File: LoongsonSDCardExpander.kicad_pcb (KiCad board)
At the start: 2 copper layers, 42.1 x 32.7 mm, 30 parts, among them J1 USB_C_Receptacle_USB2.0, J2 Micro_SD_Card_Det, J3 Conn_02x10_Odd_Even, U1 CH340E

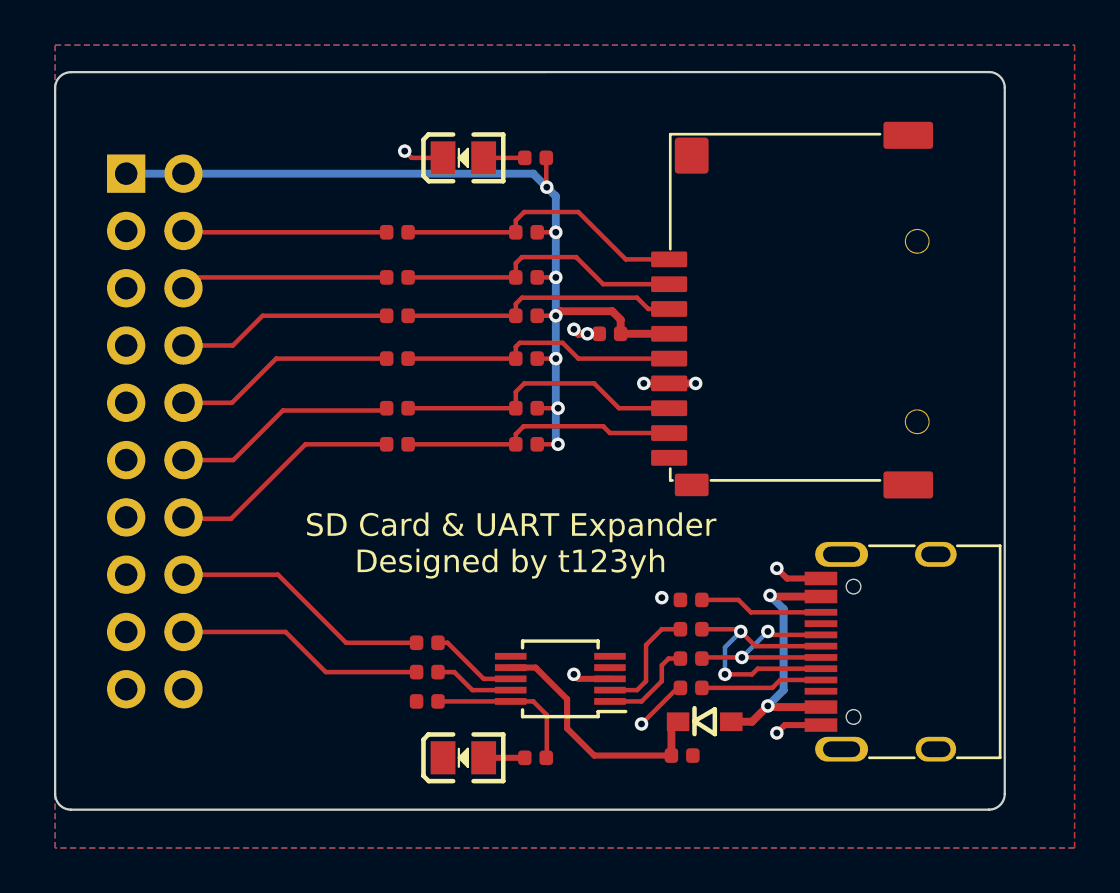
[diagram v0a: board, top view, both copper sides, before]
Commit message: 添加Conn_01x11_Socket
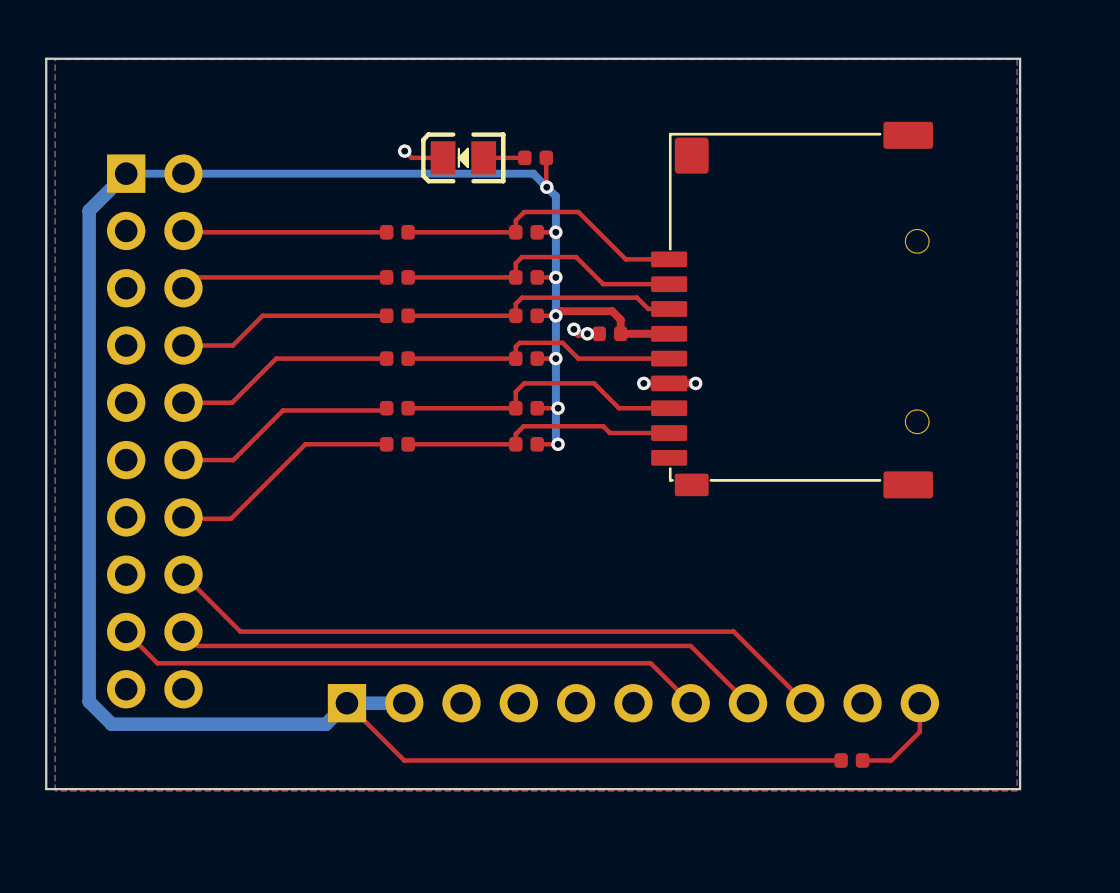
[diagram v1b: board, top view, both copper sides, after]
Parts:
- removed C1: 2.2uF, lc:0402_C
- removed C2: 100nF, lc:0402_C
- removed D1: 1N5819WS, lc:SOD-323
- removed D3: Green, lc:0805_LED_S1_NUM
- removed J1: USB_C_Receptacle_USB2.0, t123yh:USB_C_Receptacle_HRO_TYPE-C-31-M-12
- removed R1, R2: 5.1k, lc:0402_R
- removed R13, R14, R3, R4: 22, lc:0402_R
- removed R20: 22k, lc:0402_R
- removed U1: CH340E, Package_SO:MSOP-10_3x3mm_P0.5mm
- added J4: Conn_01x11_Socket, Connector_PinSocket_2.54mm:PinSocket_1x11_P2.54mm_Vertical, B.Cu at (66.0, 157.5)
- added R21: 47k, lc:0402_R, F.Cu at (88.4, 160.0)
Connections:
- J3 pad 16: /TX -> /I2S_LCK
- J3 pad 17: unconnected-(J3-Pad17) -> /I2S_BCK
- J3 pad 18: /RX -> /I2S_DIN
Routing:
- net +3.3V: track 42.8 -> 104.6 mm
- net /I2S_LCK: track 0.00 -> 29.9 mm
- net /I2S_BCK: track 0.00 -> 26.3 mm
- net /I2S_DIN: track 0.00 -> 26.3 mm
- net Net-(J1-PadA7): track 12.1 -> 0.00 mm, vias 2 -> 0
- net Net-(D1-Pad2): track 12.0 -> 0.00 mm, vias 2 -> 0
- net /TX: track 11.6 -> 0.00 mm
- net Net-(C1-Pad1): track 11.1 -> 0.00 mm
- net /RX: track 11.1 -> 0.00 mm
- net Net-(J1-PadA6): track 9.34 -> 0.00 mm, vias 2 -> 0
- net GND: track 13.6 -> 5.33 mm, vias 10 -> 5
- net Net-(C2-Pad1): track 6.98 -> 0.00 mm
- net Net-(J1-PadB5): track 5.51 -> 0.00 mm
- net Net-(J1-PadA5): track 5.42 -> 0.00 mm
- net Net-(R4-Pad2): track 5.18 -> 0.00 mm
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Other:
- board size 42.1 x 32.7 mm -> 43.2 x 32.4 mm
- board text removed: "SD Card & UART Expander Designed by t123yh"
